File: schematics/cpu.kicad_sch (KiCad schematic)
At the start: 12 parts, among them U8 W65C02SxP

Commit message: updating schematics as I wire the board
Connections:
- net RDY: now reaches R14.2, U8.2 (RDY)
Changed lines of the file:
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@@
+	)
+	(junction
+		(at 110.49 96.52)
+		(diameter 0)
+		(color 0 0 0 0)
 	)
 	(junction
@@
 		(pts
 			(xy 152.4 106.68) (xy 152.4 104.14)
+		)
+		(stroke
+			(width 0)
+			(type default)
+		)
+	)
+	(wire
+		(pts
+			(xy 107.95 96.52) (xy 110.49 96.52)
 		)
 		(stroke
@@
 			)
 		)
+	)
+	(global_label "RDY"
+		(shape input)
+		(at 107.95 96.52 180)
+		(fields_autoplaced yes)
+		(effects
+			(font
+				(size 1.27 1.27)
+			)
+			(justify right)
+		)
+		(property "Intersheetrefs" "${INTERSHEET_REFS}"
+			(at 101.3362 96.52 0)
+			(hide yes)
+			(show_name no)
+			(do_not_autoplace no)
+			(effects
+				(font
+					(size 1.27 1.27)
+				)
+				(justify right)
+			)
+		)

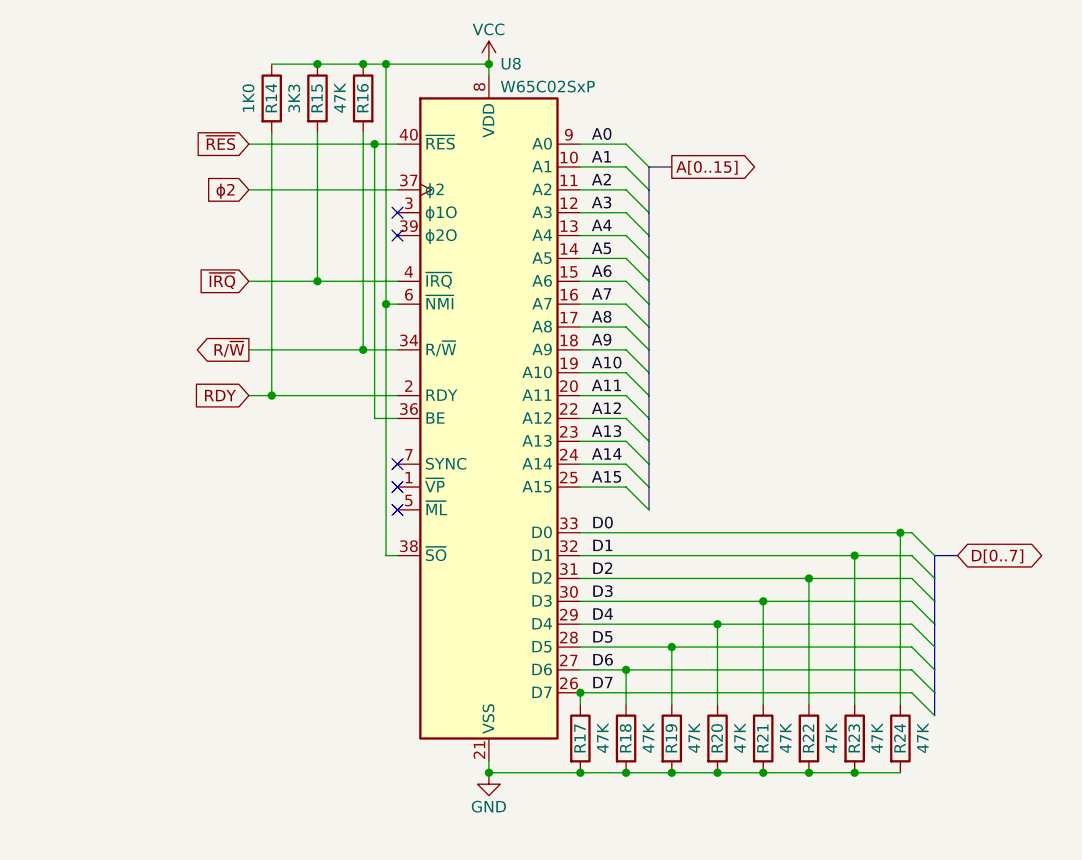
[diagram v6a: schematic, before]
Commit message: pullup/pulldown on dip switch
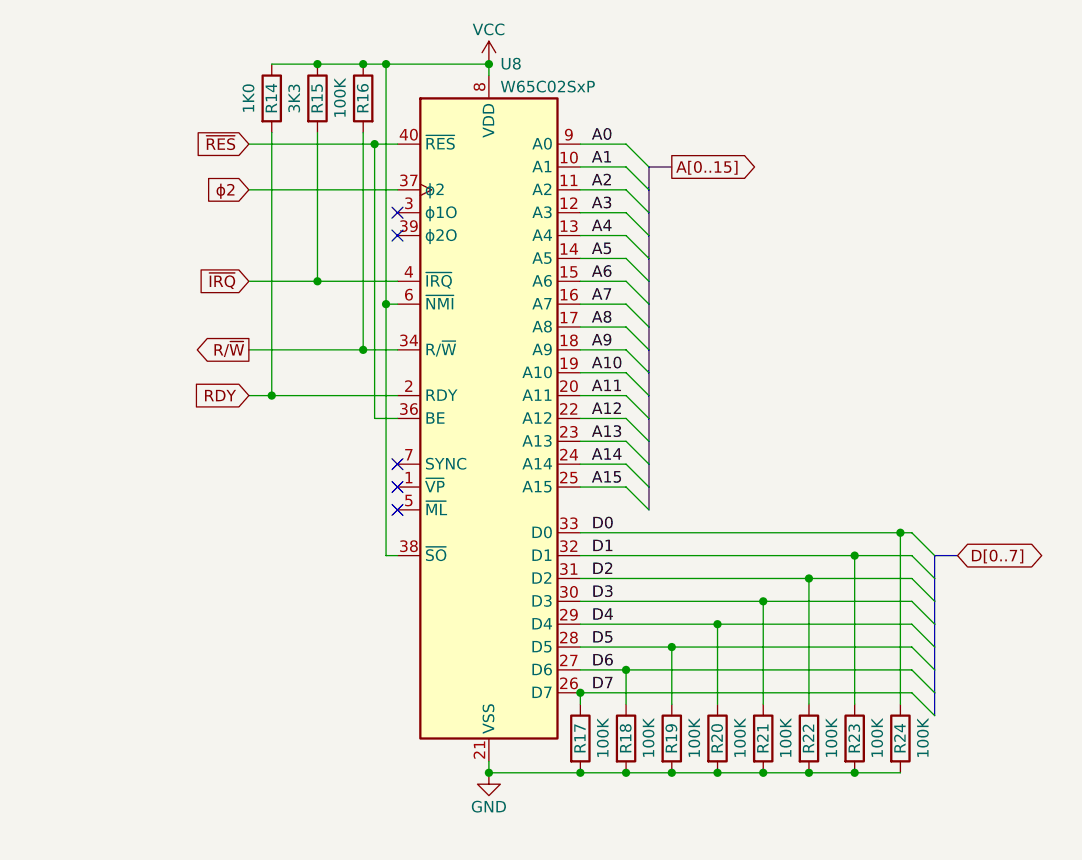
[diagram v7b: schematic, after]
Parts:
- R16, R17, R18, R19, R20, R21, R22, R23, R24: value 47K -> 100K
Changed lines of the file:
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@@
 			)
 		)
-		(property "Value" "47K"
+		(property "Value" "100K"
 			(at 177.8 134.62 90)
 			(show_name no)
@@
 			)
 		)
-		(property "Value" "47K"
+		(property "Value" "100K"
 			(at 172.72 134.62 90)
 			(show_name no)
@@
 			)
 		)
-		(property "Value" "47K"
+		(property "Value" "100K"
 			(at 162.56 134.62 90)
 			(show_name no)
@@
 			)
 		)
-		(property "Value" "47K"
+		(property "Value" "100K"
 			(at 118.11 63.5 90)
 			(show_name no)
@@
 			)
 		)
-		(property "Value" "47K"
+		(property "Value" "100K"
 			(at 147.32 134.62 90)
 			(show_name no)
@@
 			)
 		)
-		(property "Value" "47K"
+		(property "Value" "100K"
 			(at 152.4 134.62 90)
 			(show_name no)
@@
 			)
 		)
-		(property "Value" "47K"
+		(property "Value" "100K"
 			(at 182.88 134.62 90)
 			(show_name no)
@@
 			)
 		)
-		(property "Value" "47K"
+		(property "Value" "100K"
 			(at 167.64 134.62 90)
 			(show_name no)
@@
 			)
 		)
-		(property "Value" "47K"
+		(property "Value" "100K"
 			(at 157.48 134.62 90)
 			(show_name no)

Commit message: my keyboard needed a transceiver after all :(
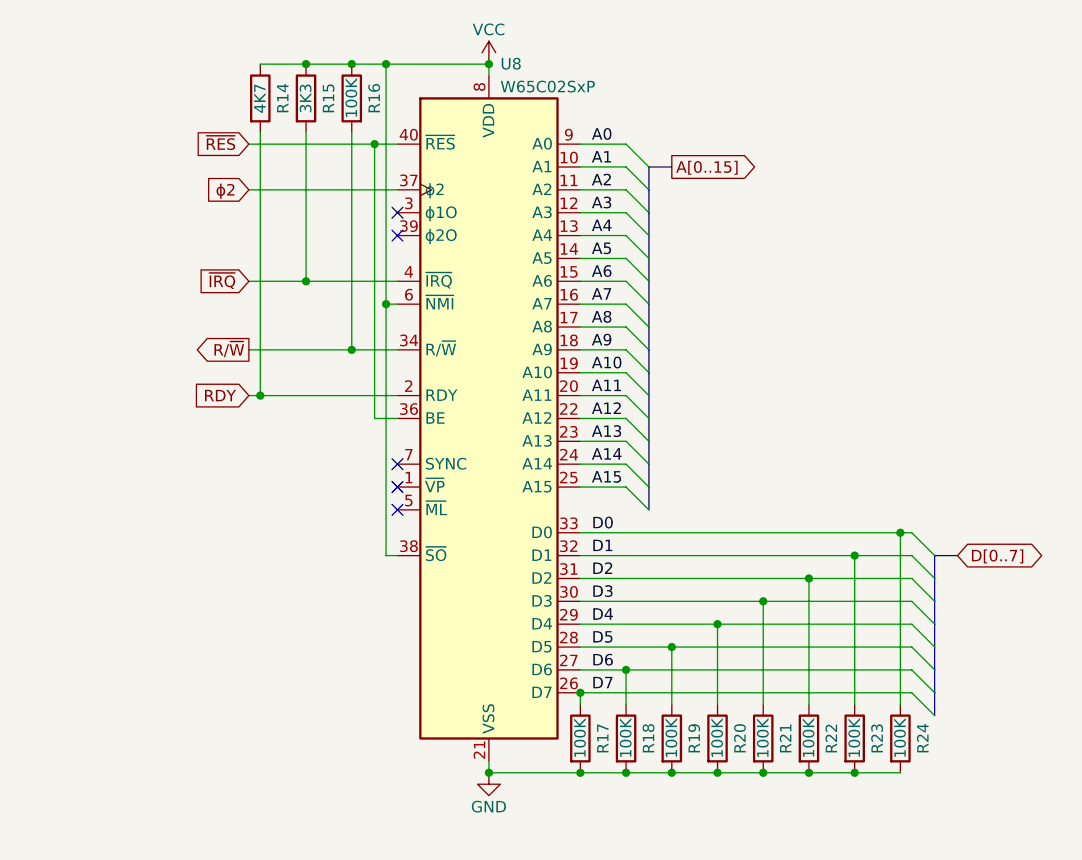
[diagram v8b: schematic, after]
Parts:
- R14: value 1K0 -> 4K7
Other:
- moved on the sheet: R14, R15, R16
